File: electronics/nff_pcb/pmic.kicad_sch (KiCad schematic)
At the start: 55 parts, among them U3 TPS62095RGTR, U4 TPS62095RGTR, U5 TPS62095RGTR, U6 TPS62095RGTR, U7 AP131-25

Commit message: R0.1 released.
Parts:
- C27: value 0.1uF -> 100nF
- TP11, TP12, TP13, TP14, TP15, TP16, TP17, TP18, TP3, TP6: now left out of the parts list
- U7: MPN AP131-25 -> AP131-25WL-7
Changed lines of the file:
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@@
 		(unit 1)
 		(exclude_from_sim no)
-		(in_bom yes)
+		(in_bom no)
 		(on_board yes)
 		(dnp no)
@@
 		(unit 1)
 		(exclude_from_sim no)
-		(in_bom yes)
+		(in_bom no)
 		(on_board yes)
 		(dnp no)
@@
 		(unit 1)
 		(exclude_from_sim no)
-		(in_bom yes)
+		(in_bom no)
 		(on_board yes)
 		(dnp no)
@@
 		(unit 1)
 		(exclude_from_sim no)
-		(in_bom yes)
+		(in_bom no)
 		(on_board yes)
 		(dnp no)
@@
 		(unit 1)
 		(exclude_from_sim no)
-		(in_bom yes)
+		(in_bom no)
 		(on_board yes)
 		(dnp no)
@@
 		(unit 1)
 		(exclude_from_sim no)
-		(in_bom yes)
+		(in_bom no)
 		(on_board yes)
 		(dnp no)
@@
 		(unit 1)
 		(exclude_from_sim no)
-		(in_bom yes)
+		(in_bom no)
 		(on_board yes)
 		(dnp no)
@@
 			)
 		)
-		(property "Value" "0.1uF"
+		(property "Value" "100nF"
 			(at 146.05 161.29 0)
 			(effects
@@
 		(unit 1)
 		(exclude_from_sim no)
-		(in_bom yes)
+		(in_bom no)
 		(on_board yes)
 		(dnp no)
@@
 		(unit 1)
 		(exclude_from_sim no)
-		(in_bom yes)
+		(in_bom no)
 		(on_board yes)
 		(dnp no)
@@
 			)
 		)
-		(property "MPN" "AP131-25"
+		(property "MPN" "AP131-25WL-7"
 			(at 135.89 154.94 0)
 			(effects
@@
 		(unit 1)
 		(exclude_from_sim no)
-		(in_bom yes)
+		(in_bom no)
 		(on_board yes)
 		(dnp no)

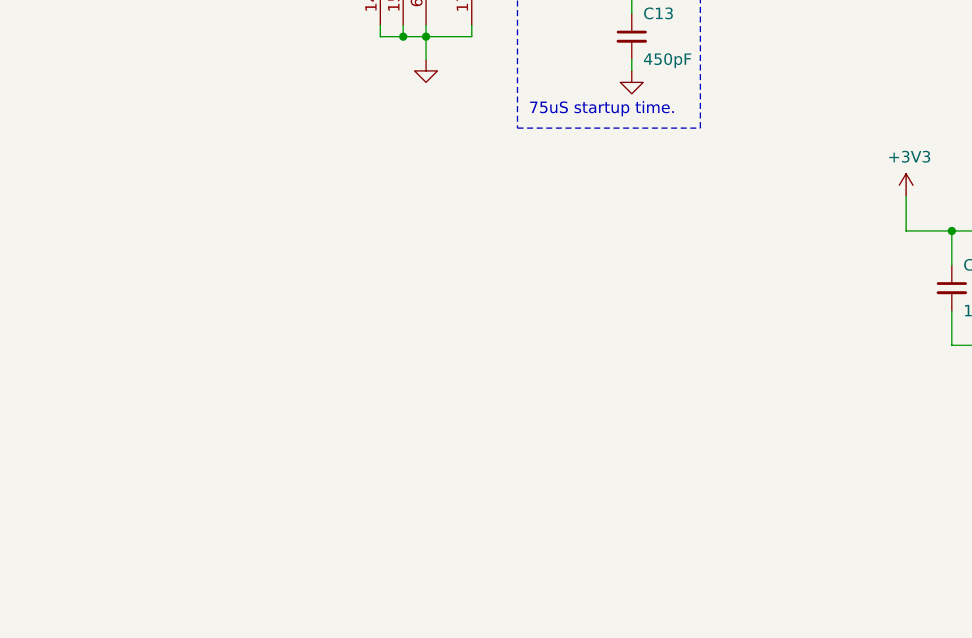
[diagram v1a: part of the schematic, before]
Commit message: “or” the 5V line, “or” the UART bus, reroute the PWM line to be actually PWM, Reset button., Decoup caps over USB.
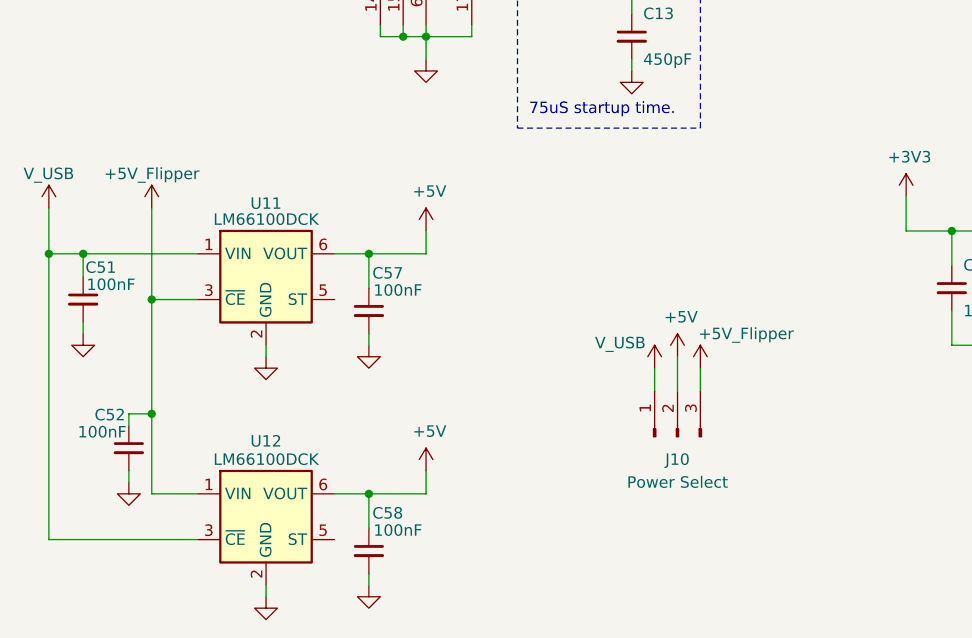
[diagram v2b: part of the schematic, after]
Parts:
- added C51, C52, C57, C58: 100nF, Capacitor_SMD:C_0402_1005Metric, symbol Device:C_Small
- added J10: Power Select, Connector_PinHeader_2.54mm:PinHeader_1x03_P2.54mm_Vertical, symbol Connector:Conn_01x03_Pin
- added U11, U12: LM66100DCK, Package_TO_SOT_SMD:SOT-363_SC-70-6, symbol Power_Management:LM66100DCK
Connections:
- net +5V: now also C57.1, C58.1, J10.2 (Pin_2), U11.6 (VOUT), U12.6 (VOUT)
- net GND: now also C51.2, C52.2, C57.2, C58.2, U11.2 (GND), U12.2 (GND)
- new net +5V_Flipper: C52.1, J10.3 (Pin_3), U11.3 (~{CE}), U12.1 (VIN)
- new net V_USB: C51.1, J10.1 (Pin_1), U11.1 (VIN), U12.3 (~{CE})

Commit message: R2 Released
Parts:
- removed R15, R16, R17, R18, R19: 0R, Resistor_SMD:R_0402_1005Metric, symbol Device:R_Small_US
- removed TP11, TP12, TP17, TP3, TP6: TestPoint, TestPoint:TestPoint_Pad_1.0x1.0mm, symbol Connector:TestPoint
- C27: now not fitted
- L1, L2, L3, L4: footprint Inductor_SMD:L_Coilcraft_XxL4020 -> SNH.4020.TYB1R0MT00:SNH.4020.TYB1R0MT00; MPN XAL4020-102ME -> SNH.4020.TYB1R0MT00
- U11, U12: MPN (none) -> LM66100DCKR
- U7: MPN AP131-25WL-7 -> AP7331-25WG-7
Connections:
- net +1V1: now also C23.1, C25.1, L4.2, R13.1, U6.16 (VOS)
- net +1V35: now also C22.1, C24.1, L3.2, R11.1, U5.16 (VOS)
- net +2V5: now also C28.1, U7.5 (OUT)
- net +3V0: now also C14.1, C15.1, L2.2, R9.1, U4.16 (VOS)
- net +3V3: now also C10.1, C9.1, L1.2, R7.1, U3.16 (VOS)
